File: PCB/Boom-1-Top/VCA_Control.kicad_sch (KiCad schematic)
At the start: 66 parts, among them J45 FXConn2, U43 V2164D, U44 V2164D, U45 TL074, U46 TL074, U47 TL074, U50 DAC7678xPW, U57 24LC32

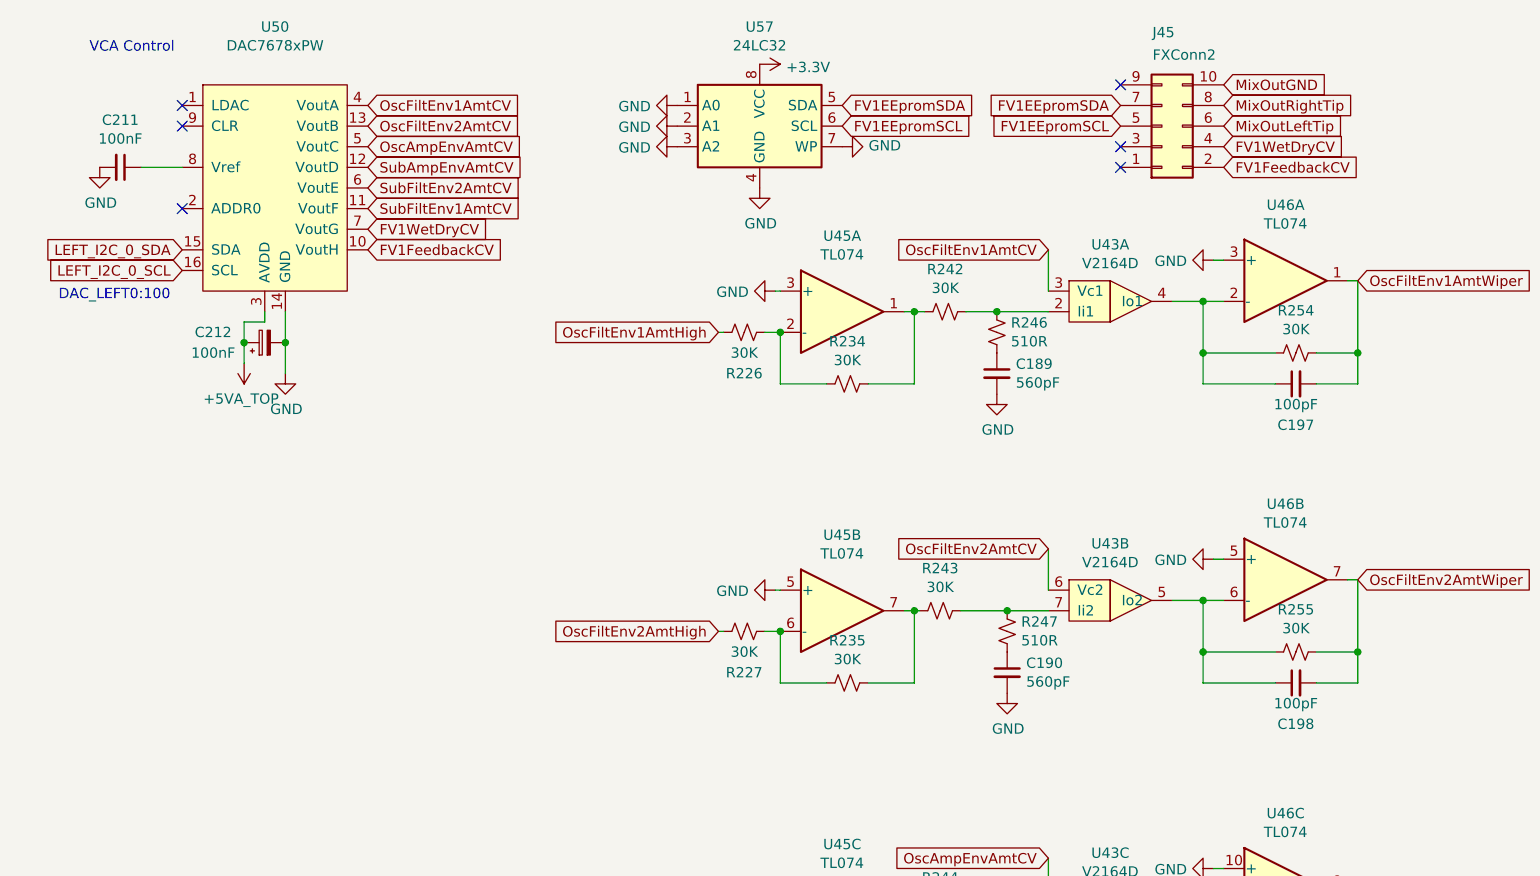
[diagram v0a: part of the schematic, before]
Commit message: Top: done splitting up the DAC-related parts
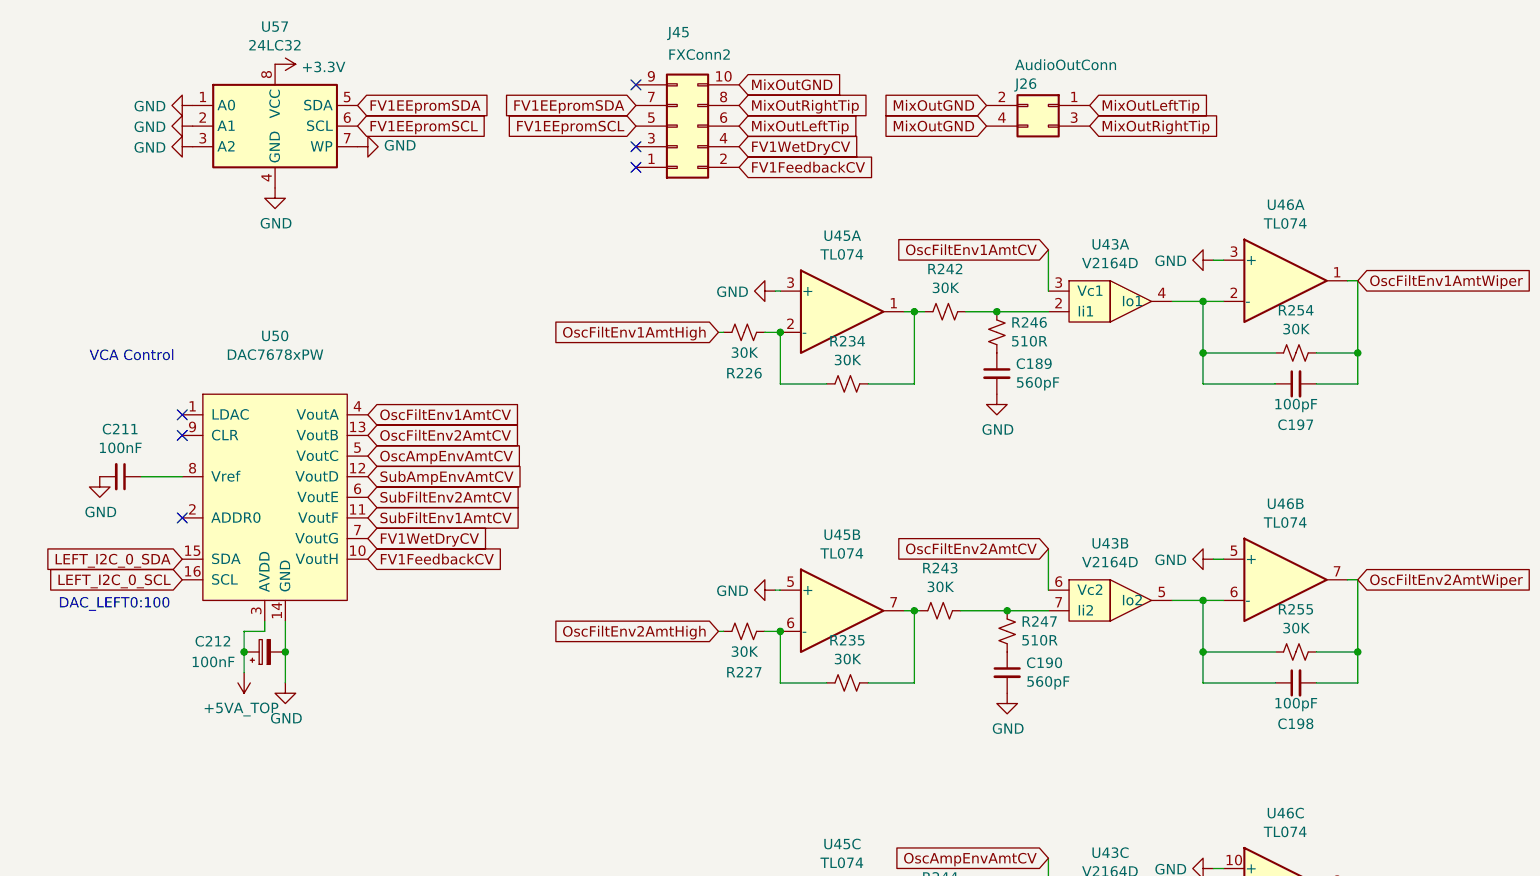
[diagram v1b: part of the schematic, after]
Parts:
- added J26: AudioOutConn, Connector_PinSocket_2.54mm:PinSocket_2x02_P2.54mm_Vertical, symbol Connector_Generic:Conn_02x02_Odd_Even
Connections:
- net MixOutGND: now also J26.2 (Pin_2), J26.4 (Pin_4)
- net MixOutLeftTip: now also J26.1 (Pin_1)
- net MixOutRightTip: now also J26.3 (Pin_3)
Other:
- moved on the sheet: C211, C212, J45, U50, U57
